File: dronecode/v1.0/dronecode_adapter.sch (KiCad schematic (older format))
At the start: 9 parts, among them J1 Jumper, J2 Jumper, J3 Jumper, J4 Jumper, X1 JTAG-10

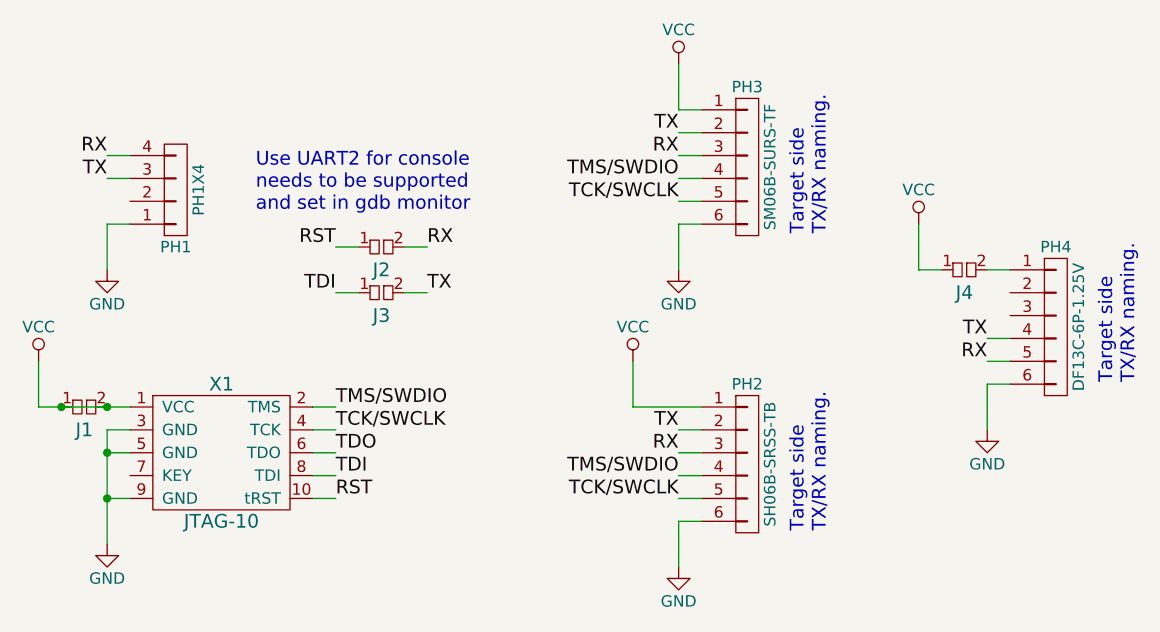
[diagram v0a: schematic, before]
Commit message: Some name corrections.
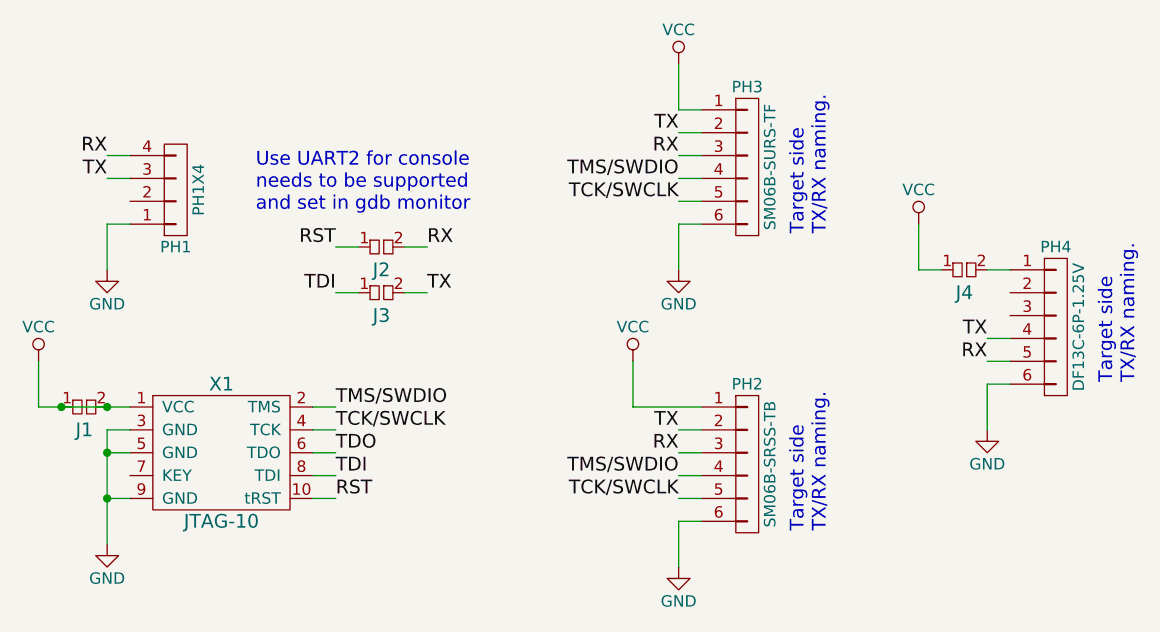
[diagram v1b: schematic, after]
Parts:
- PH2: value SH06B-SRSS-TB -> SM06B-SRSS-TB
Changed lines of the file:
@@
 P 7050 3500
 F 0 "PH2" H 7050 3850 50  0000 C CNN
-F 1 "SH06B-SRSS-TB" V 7150 3500 50  0000 C CNN
+F 1 "SM06B-SRSS-TB" V 7150 3500 50  0000 C CNN
 F 2 "Connectors_JST_SH:Connectors_JST_SM06B-SRSS-TB" H 7050 3600 60  0001 C CNN
 F 3 "" H 7050 3600 60  0000 C CNN

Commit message: Updated jumper symbols in dronecode adapter.
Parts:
- J1, J2, J3, J4: symbol Jumper -> pkl_jumper
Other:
- moved on the sheet: PH1
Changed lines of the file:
@@
 EESchema Schematic File Version 2
+LIBS:dronecode_adapter-rescue
 LIBS:power
 LIBS:device
@@
 L PH1X4 PH1
 U 1 1 56B30FD5
-P 4550 2300
-F 0 "PH1" H 4550 2550 50  0000 C CNN
-F 1 "PH1X4" V 4650 2300 50  0000 C CNN
-F 2 "Connectors_Molex:Connector_Molex_PicoBlade_53261-0471" H 4550 2300 60  0001 C CNN
-F 3 "" H 4550 2300 60  0000 C CNN
-F 4 "ANY" H 4550 2300 60  0001 C CNN "Source"
-	1    4550 2300
-	1    0    0    1
-$EndComp
-Wire Wire Line
-	4350 2450 4250 2450
-Wire Wire Line
-	4250 2450 4250 2650
+P 4250 2300
+F 0 "PH1" H 4250 2550 50  0000 C CNN
+F 1 "PH1X4" V 4350 2300 50  0000 C CNN
+F 2 "Connectors_Molex:Connector_Molex_PicoBlade_53261-0471" H 4250 2300 60  0001 C CNN
+F 3 "" H 4250 2300 60  0000 C CNN
+F 4 "ANY" H 4250 2300 60  0001 C CNN "Source"
+	1    4250 2300
+	-1   0    0    1
+$EndComp
+Wire Wire Line
+	4450 2450 4550 2450
+Wire Wire Line
+	4550 2450 4550 2650
 $Comp
 L GND #PWR03
 U 1 1 56B31064
-P 4250 2650
-F 0 "#PWR03" H 4250 2400 50  0001 C CNN
-F 1 "GND" H 4250 2500 50  0000 C CNN
-F 2 "" H 4250 2650 50  0000 C CNN
-F 3 "" H 4250 2650 50  0000 C CNN
-	1    4250 2650
-	1    0    0    -1
-$EndComp
-Wire Wire Line
-	4350 2250 4250 2250
-Wire Wire Line
-	4350 2150 4250 2150
-Text Label 4250 2250 2    60   ~ 0
+P 4550 2650
+F 0 "#PWR03" H 4550 2400 50  0001 C CNN
+F 1 "GND" H 4550 2500 50  0000 C CNN
+F 2 "" H 4550 2650 50  0000 C CNN
+F 3 "" H 4550 2650 50  0000 C CNN
+	1    4550 2650
+	-1   0    0    -1
+$EndComp
+Wire Wire Line
+	4450 2250 4550 2250
+Wire Wire Line
+	4450 2150 4550 2150
+Text Label 4550 2250 0    60   ~ 0
 TX
-Text Label 4250 2150 2    60   ~ 0
+Text Label 4550 2150 0    60   ~ 0
 RX
 $Comp
@@
 TX
 $Comp
-L Jumper J1
+L pkl_jumper J1
 U 1 1 56B54FEC
 P 4150 3250
@@
 $EndComp
 $Comp
-L Jumper J4
+L pkl_jumper J4
 U 1 1 56B55473
 P 8000 2650
@@
 RX
 $Comp
-L Jumper J2
+L pkl_jumper J2
 U 1 1 56B55643
 P 5450 2550
@@
 $EndComp
 $Comp
-L Jumper J3
+L pkl_jumper J3
 U 1 1 56B5575F
 P 5450 2750
